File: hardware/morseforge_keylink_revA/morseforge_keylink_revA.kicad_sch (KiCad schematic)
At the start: 20 parts, among them J1 USB_C_Receptacle_USB2.0_14P, J2 Conn_01x02_Socket, SW1 SW_SPST, U1 MCP73831-2-MC, U2 LDO40LPU33RY, U3 CP2102N-Axx-xQFN20

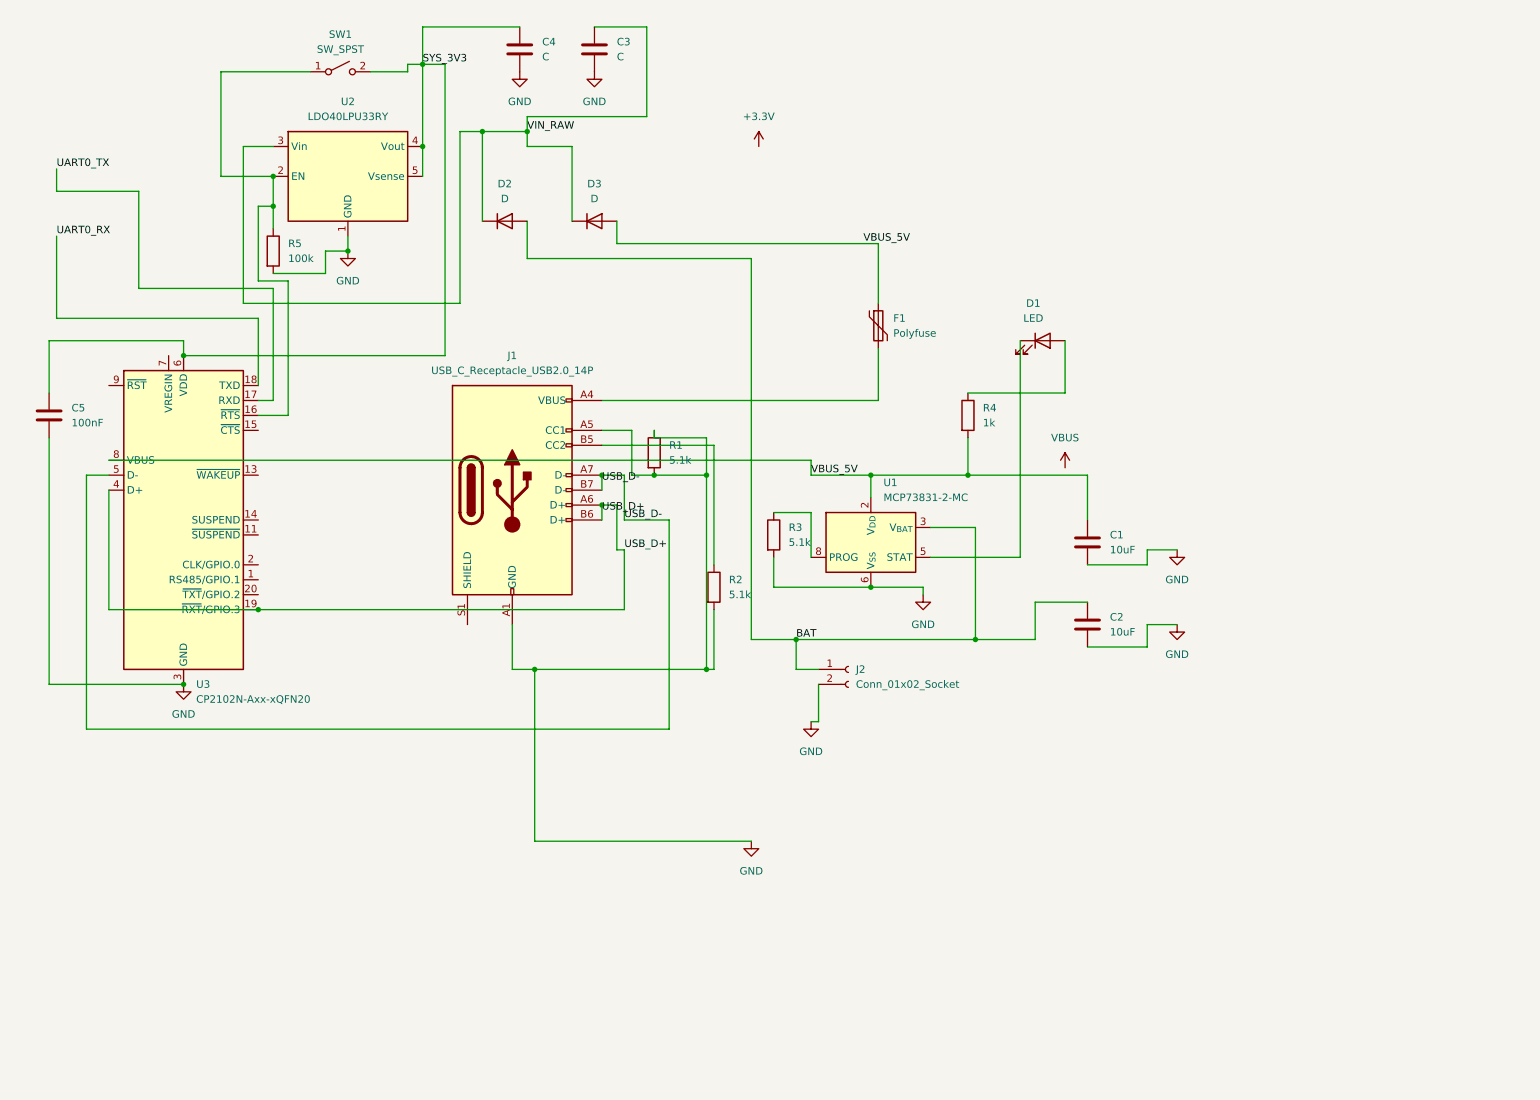
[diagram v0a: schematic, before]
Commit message: Adding reset and boot buttons
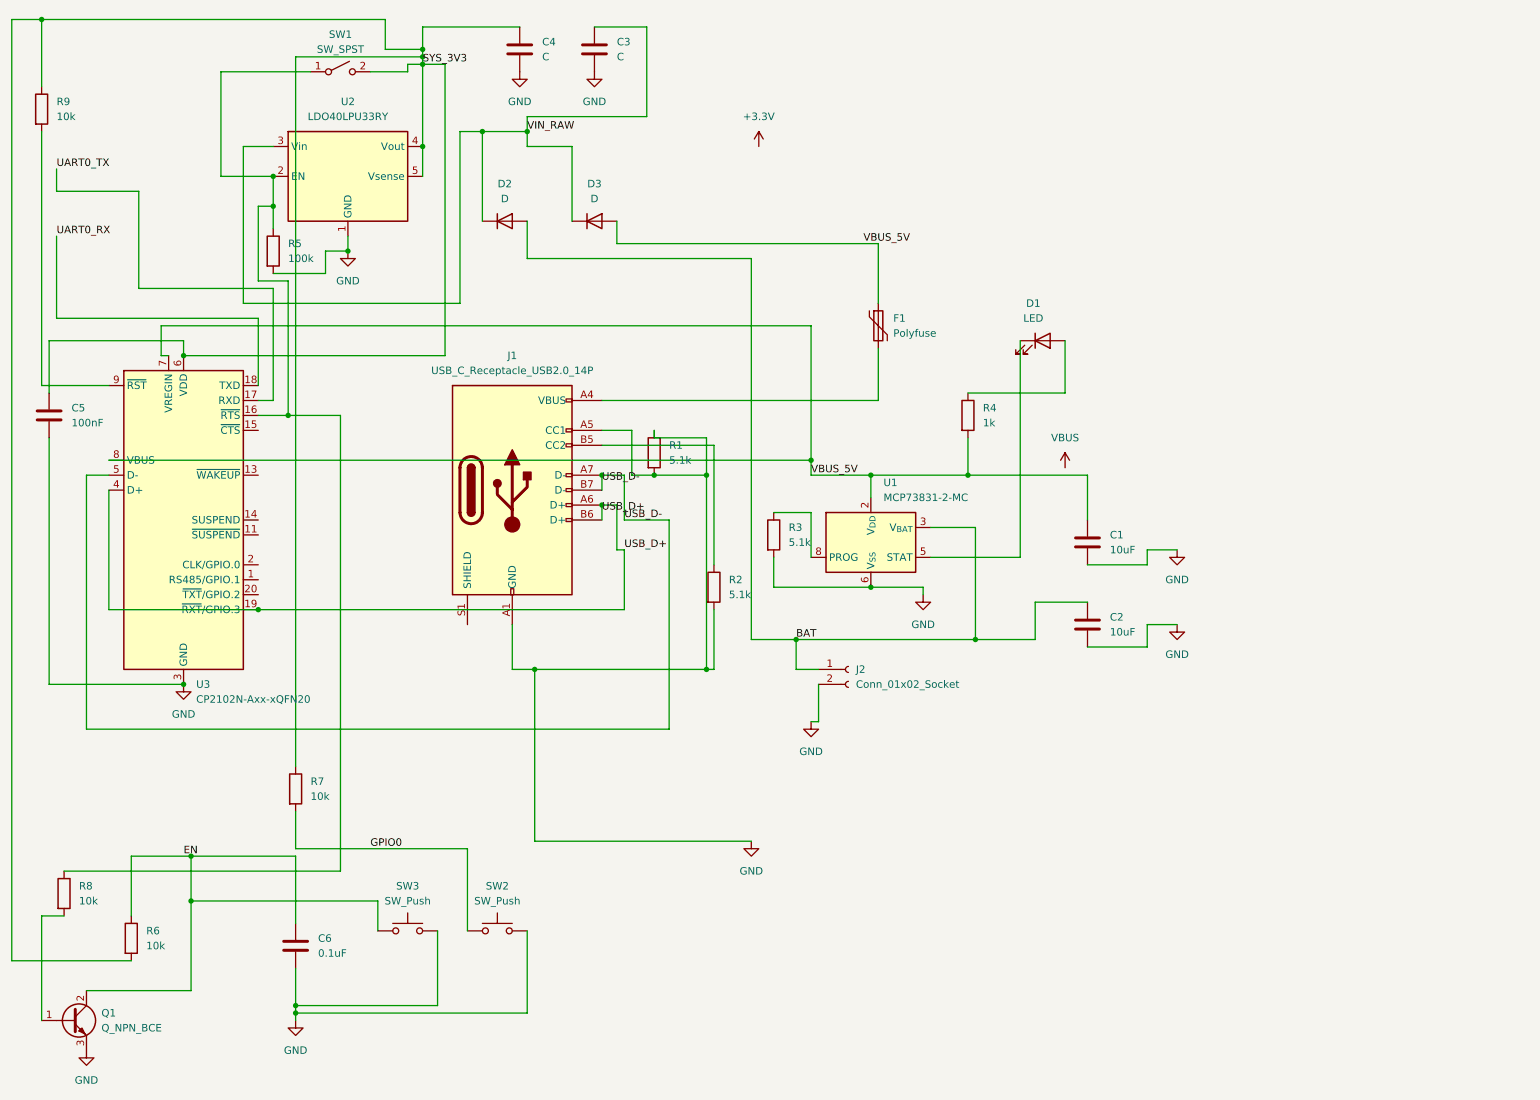
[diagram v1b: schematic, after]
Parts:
- added C6: 0.1uF, symbol Device:C
- added Q1: Q_NPN_BCE, symbol Transistor_BJT:Q_NPN_BCE
- added R6, R7, R8, R9: 10k, symbol Device:R
- added SW2, SW3: SW_Push, symbol Switch:SW_Push
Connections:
- net GND: now also C6.2, Q1.3 (E), SW2.2, SW3.2
- net SYS_3V3: now also R6.2, R7.1, R9.1
- net VBUS_5V: now also U3.7 (VREGIN)
- net at R5.1, SW1.1 (A), U2.2 (EN)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: now also R8.1
- net at U3.9 (~{RST}): now also R9.2
- new net: Q1.1 (B), R8.2
- new net EN: C6.1, Q1.2 (C), R6.1, SW3.1
- new net GPIO0: R7.2, SW2.1

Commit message: Adding in esp32
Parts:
- added U4: ESP32-WROOM-32, RF_Module:ESP32-WROOM-32, symbol RF_Module:ESP32-WROOM-32
- U3: footprint Package_DFN_QFN:SiliconLabs_QFN-20-1EP_3x3mm_P0.5mm -> Package_DFN_QFN:QFN-20-1EP_3x3mm_P0.45mm_EP1.6x1.6mm
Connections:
- net EN: now also U4.3 (EN)
- net GND: now also U4.1 (GND), U4.15 (GND), U4.38 (GND), U4.39 (GND)
- net GPIO0: now also U4.25 (IO0)
- net SYS_3V3: now also U4.2 (VDD)
- net UART0_RX: now also U4.34 (RXD0/IO3)
- net UART0_TX: now also U4.35 (TXD0/IO1)
- new net BTN_USER: U4.8 (IO32)
- new net DAH_IN: U4.12 (IO27)
- new net DIT_IN: U4.13 (IO14)
- new net GPIO33_SPARE: U4.9 (IO33)
- new net LED_B: U4.37 (IO23)
- new net LED_G: U4.36 (IO22)
- new net LED_R: U4.33 (IO21)

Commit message: rev b board, much simpler
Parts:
- added C7, C8: 10nF, Capacitor_SMD:C_0603_1608Metric, symbol Device:C
- added D5: LED_RGB, LED_SMD:LED_RGB_5050-6, symbol Device:LED_RGB
- added J3: AudioJack4, Connector_Audio:Jack_3.5mm_PJ320D_Horizontal, symbol Connector_Audio:AudioJack4
- added J4: Conn_01x01_Pin, TestPoint:TestPoint_Pad_D1.0mm, symbol Connector:Conn_01x01_Pin
- added R10, R11, R12: 330, Resistor_SMD:R_0603_1608Metric, symbol Device:R
- added SW4: SW_Push, Button_Switch_SMD:SW_SPST_TL3342, symbol Switch:SW_Push
- C1, C2, C3, C4, C5, C6: footprint (none) -> Capacitor_SMD:C_0603_1608Metric
- D1, D2, D3: footprint (none) -> Diode_SMD:D_SOD-123
- F1: footprint (none) -> Fuse:Fuse_1206_3216Metric
- J1: footprint (none) -> Connector_USB:USB_C_Receptacle_GCT_USB4105-xx-A_16P_TopMnt_Horizontal
- J2: footprint (none) -> Connector_JST:JST_PH_S2B-PH-K_1x02_P2.00mm_Horizontal
- Q1: footprint (none) -> Package_TO_SOT_SMD:SOT-23-5_HandSoldering
- R1, R2, R3, R4, R5, R6, R7, R8, R9: footprint (none) -> Resistor_SMD:R_0603_1608Metric
- SW1: footprint (none) -> Button_Switch_THT:SW_Slide-03_Wuerth-WS-SLTV_10x2.5x6.4_P2.54mm
- SW2, SW3: footprint (none) -> Button_Switch_SMD:SW_SPST_TL3342
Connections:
- net BTN_USER: now also SW4.2
- net DAH_IN: now also C7.2, J3.R1
- net DIT_IN: now also C8.2, J3.T
- net GND: now also J1.S1 (SHIELD), C7.1, C8.1, D5.4 (BA), D5.5 (GA), D5.6 (RA), J3.S, SW4.1
- net GPIO33_SPARE: now also J4.1 (Pin_1)
- net LED_B: now also R12.1
- net LED_G: now also R11.1
- net LED_R: now also R10.1
- new net: D5.1 (RK), R10.2
- new net: D5.2 (GK), R11.2
- new net: D5.3 (BK), R12.2
- no-connect marks 0 -> 30
